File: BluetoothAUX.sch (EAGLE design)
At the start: 17 parts, among them IC2 TPA6132A2, X1 STEREOJACK, X2 MINI-USB-SCHIELD-32005-201

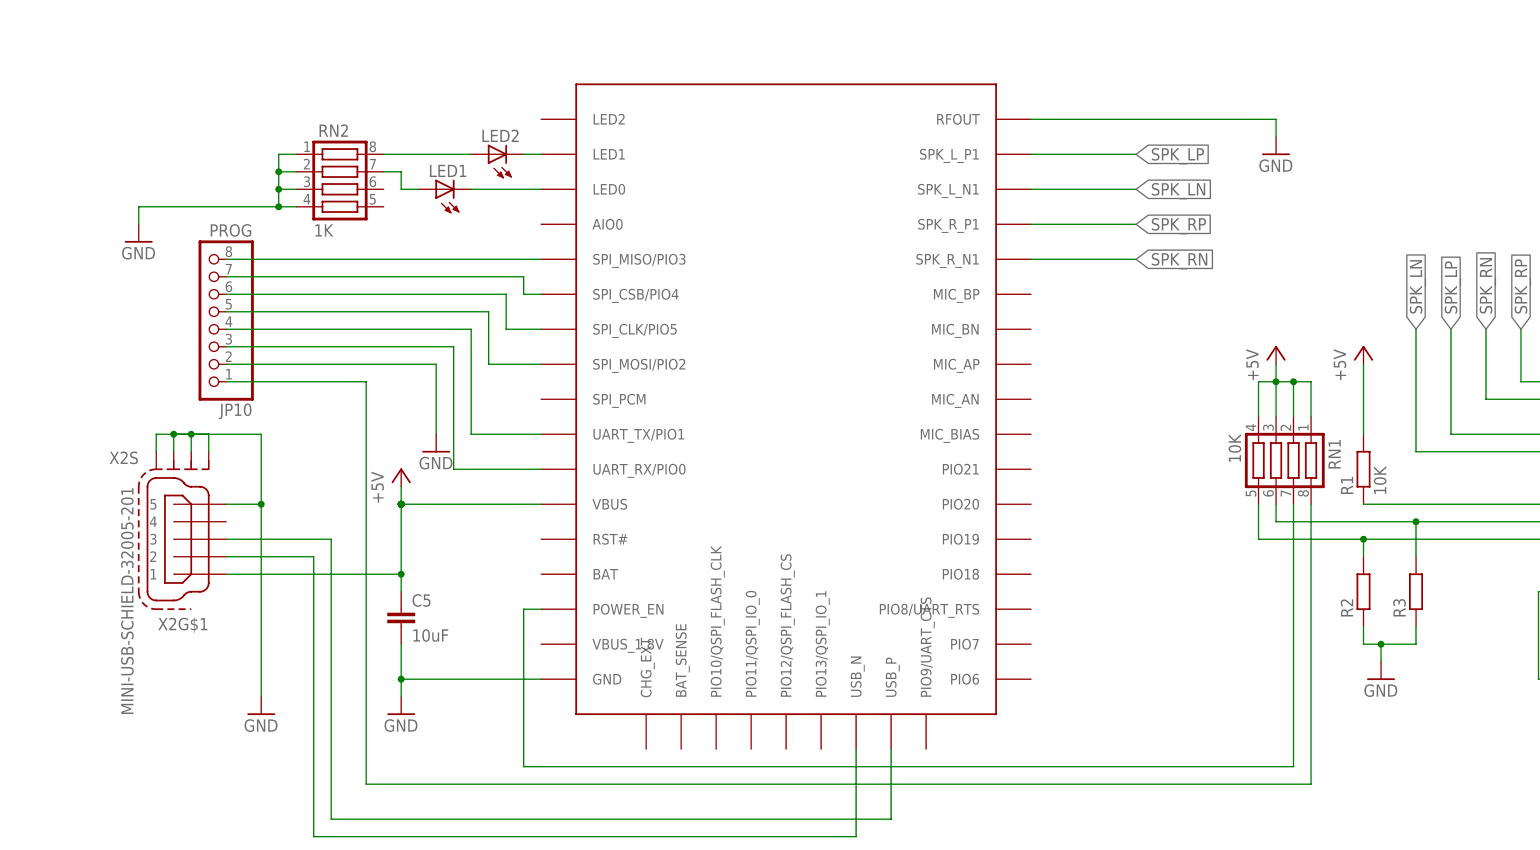
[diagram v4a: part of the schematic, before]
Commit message: Proper RN symbols
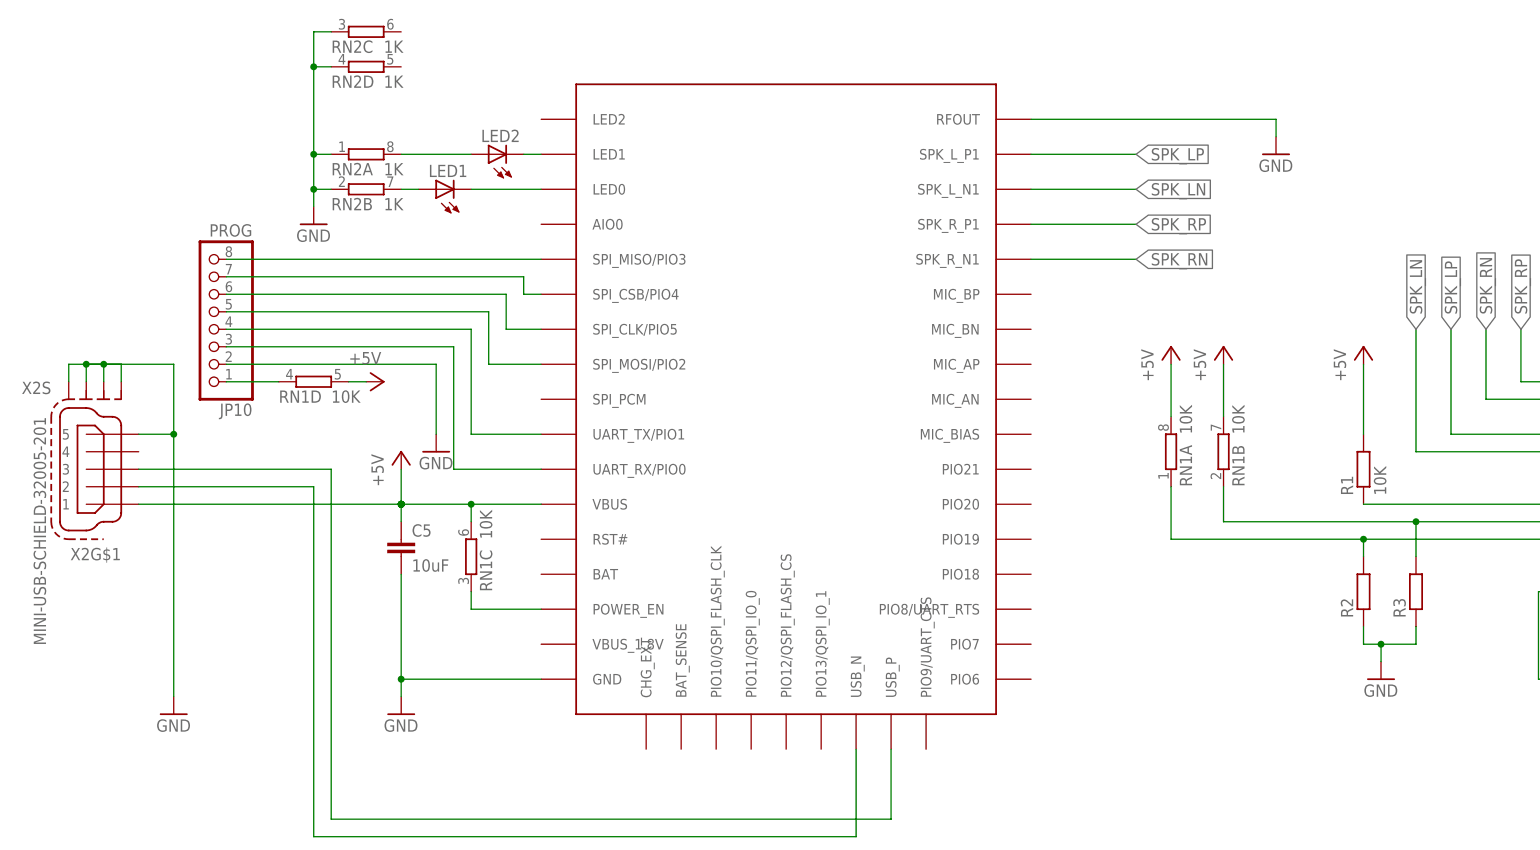
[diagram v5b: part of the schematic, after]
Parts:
- RN1, RN2: device resistor-net:CTS742C083 -> resistor-dil:4R-N0603-ARC
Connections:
- net +5V: now also RN1A.2, RN1B.2, RN1C.2, RN1D.2; no longer RN1.1, RN1.2, RN1.3, RN1.4
- net COM: now also RN1D.1; no longer RN1.8
- net GND: now also RN2A.1, RN2B.1, RN2C.1, RN2D.1; no longer RN2.1, RN2.2, RN2.3, RN2.4
- net LED1-: now also RN2B.2; no longer RN2.7
- net LED2-: now also RN2A.2; no longer RN2.8
- net N$13: now also RN1C.1; no longer RN1.7
- net N$31: now also RN1B.1; no longer RN1.6
- net N$32: now also RN1A.1; no longer RN1.5
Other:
- moved on the sheet: C5, X2G$1, X2S

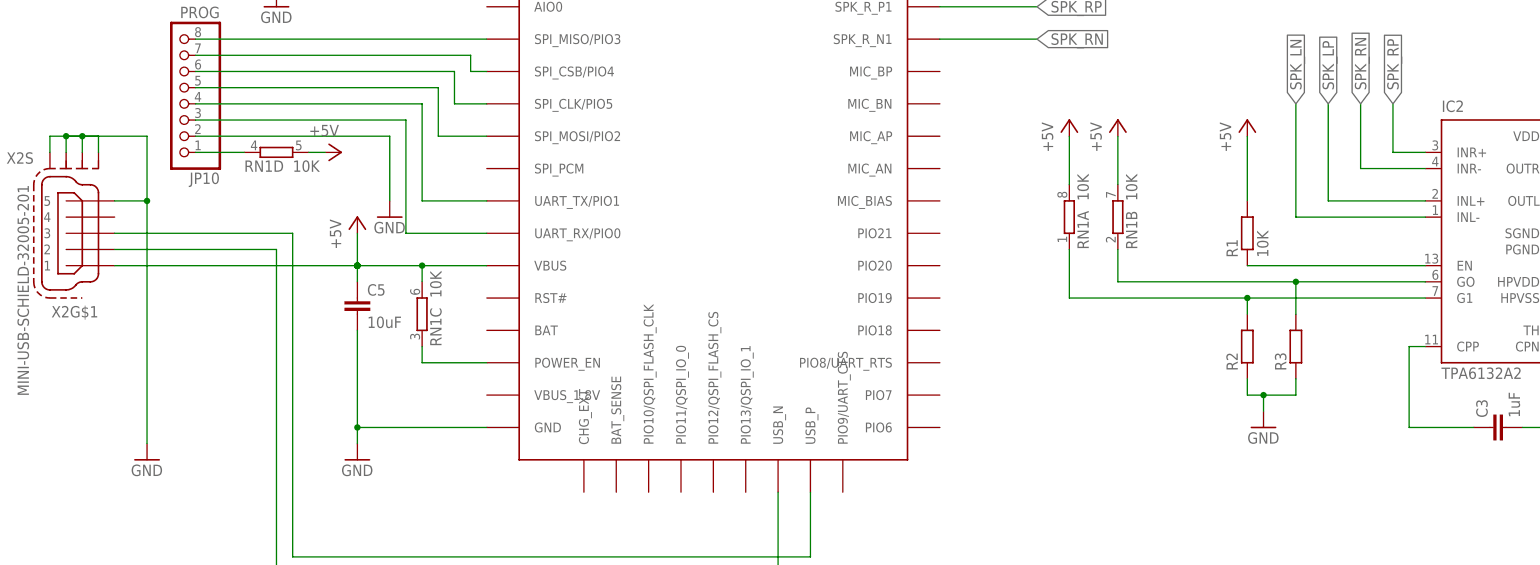
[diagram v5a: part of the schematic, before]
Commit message: Remove unused COM pin
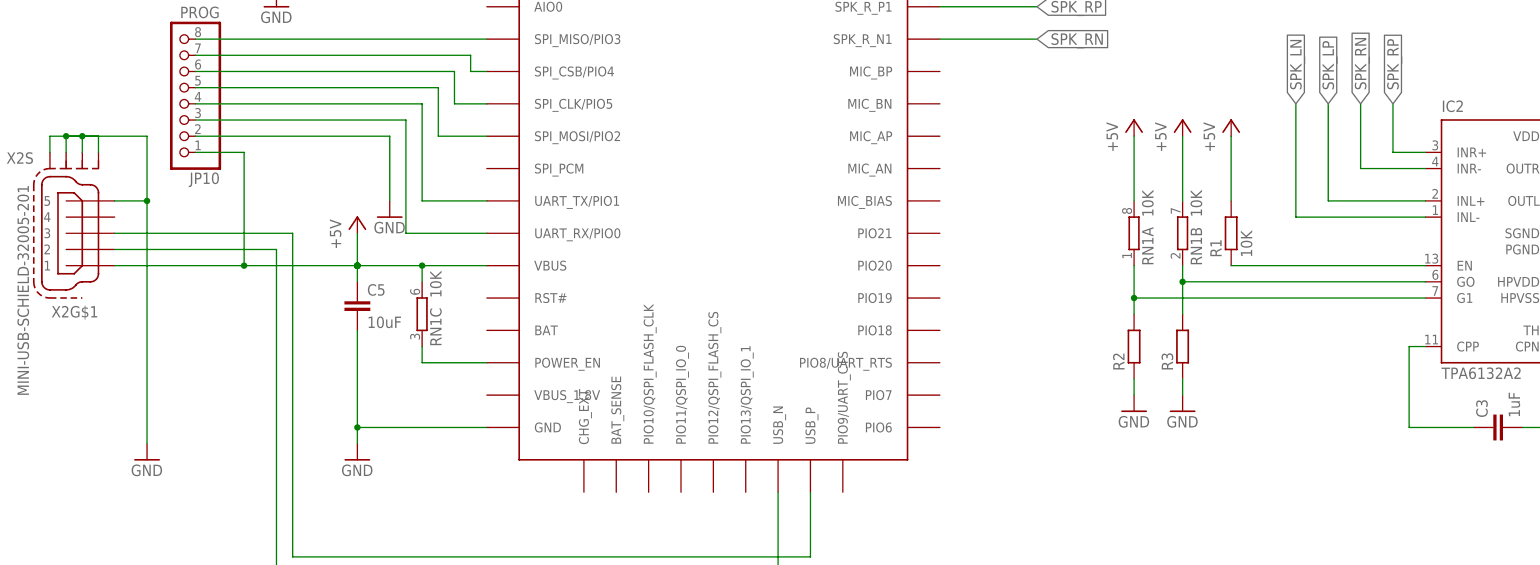
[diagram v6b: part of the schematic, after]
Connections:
- removed net COM: JP10.1, RN1D.1
- net +5V: now also JP10.1; no longer RN1D.2
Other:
- moved on the sheet: R1, R2, R3, RN1A, RN1B
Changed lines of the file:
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@@
 <part name="RN2" library="resistor-dil" library_urn="urn:adsk.eagle:library:342" deviceset="4R-N" device="0603-ARC" package3d_urn="urn:adsk.eagle:package:24926/1" value="1K"/>
 <part name="P+2" library="supply1" deviceset="+5V" device=""/>
-<part name="P+7" library="supply1" deviceset="+5V" device=""/>
+<part name="GND4" library="supply1" deviceset="GND" device=""/>
 </parts>
 <sheets>
@@
 <instance part="GND11" gate="1" x="58.42" y="-33.02"/>
 <instance part="GND12" gate="1" x="68.58" y="-33.02"/>
-<instance part="P+5" gate="1" x="-12.7" y="12.7"/>
-<instance part="P+6" gate="1" x="-33.02" y="12.7"/>
-<instance part="GND14" gate="1" x="-10.16" y="-35.56"/>
-<instance part="R2" gate="G$1" x="-12.7" y="-22.86" rot="R90"/>
-<instance part="R3" gate="G$1" x="-5.08" y="-22.86" rot="R90"/>
+<instance part="P+5" gate="1" x="-15.24" y="12.7"/>
+<instance part="P+6" gate="1" x="-22.86" y="12.7"/>
+<instance part="GND14" gate="1" x="-30.48" y="-33.02"/>
+<instance part="R2" gate="G$1" x="-30.48" y="-22.86" rot="R90"/>
+<instance part="R3" gate="G$1" x="-22.86" y="-22.86" rot="R90"/>
 <instance part="C1" gate="G$1" x="48.26" y="-20.32"/>
 <instance part="C2" gate="G$1" x="58.42" y="-20.32"/>
 <instance part="C3" gate="G$1" x="25.4" y="-35.56" rot="R90"/>
-<instance part="R1" gate="G$1" x="-12.7" y="-5.08" rot="R90"/>
+<instance part="R1" gate="G$1" x="-15.24" y="-5.08" rot="R90"/>
 <instance part="C4" gate="G$1" x="48.26" y="17.78"/>
 <instance part="GND1" gate="1" x="48.26" y="7.62"/>
@@
 <instance part="LED1" gate="G$1" x="-147.32" y="35.56" rot="R90"/>
 <instance part="GND2" gate="1" x="-165.1" y="30.48"/>
-<instance part="RN1" gate="A" x="-40.64" y="-2.54" rot="R90"/>
-<instance part="RN1" gate="B" x="-33.02" y="-2.54" rot="R90"/>
+<instance part="RN1" gate="A" x="-30.48" y="-5.08" rot="R90"/>
+<instance part="RN1" gate="B" x="-22.86" y="-5.08" rot="R90"/>
 <instance part="RN1" gate="C" x="-142.24" y="-17.78" rot="R90"/>
-<instance part="RN1" gate="D" x="-165.1" y="7.62"/>
 <instance part="RN2" gate="A" x="-157.48" y="40.64"/>
 <instance part="RN2" gate="B" x="-157.48" y="35.56"/>
 <instance part="RN2" gate="C" x="-157.48" y="58.42"/>
 <instance part="RN2" gate="D" x="-157.48" y="53.34"/>
-<instance part="P+2" gate="1" x="-40.64" y="12.7"/>
-<instance part="P+7" gate="1" x="-154.94" y="7.62" rot="R270"/>
+<instance part="P+2" gate="1" x="-30.48" y="12.7"/>
+<instance part="GND4" gate="1" x="-22.86" y="-33.02"/>
 </instances>
 <busses>
@@
 <segment>
 <pinref part="GND14" gate="1" pin="GND"/>
-<pinref part="R3" gate="G$1" pin="1"/>
-<wire x1="-10.16" y1="-30.48" x2="-10.16" y2="-33.02" width="0.1524" layer="91"/>
 <pinref part="R2" gate="G$1" pin="1"/>
-<wire x1="-12.7" y1="-27.94" x2="-12.7" y2="-30.48" width="0.1524" layer="91"/>
-<wire x1="-10.16" y1="-30.48" x2="-12.7" y2="-30.48" width="0.1524" layer="91"/>
-<junction x="-10.16" y="-30.48"/>
-<wire x1="-10.16" y1="-30.48" x2="-5.08" y2="-30.48" width="0.1524" layer="91"/>
-<wire x1="-5.08" y1="-30.48" x2="-5.08" y2="-27.94" width="0.1524" layer="91"/>
+<wire x1="-30.48" y1="-27.94" x2="-30.48" y2="-30.48" width="0.1524" layer="91"/>
 </segment>
 <segment>
@@
 <junction x="-165.1" y="53.34"/>
 </segment>
+<segment>
+<pinref part="R3" gate="G$1" pin="1"/>
+<pinref part="GND4" gate="1" pin="GND"/>
+<wire x1="-22.86" y1="-30.48" x2="-22.86" y2="-27.94" width="0.1524" layer="91"/>
+</segment>
 </net>
 <net name="+5V" class="1">
@@
 <segment>
 <pinref part="P+5" gate="1" pin="+5V"/>
-<wire x1="-12.7" y1="10.16" x2="-12.7" y2="0" width="0.1524" layer="91"/>
+<wire x1="-15.24" y1="10.16" x2="-15.24" y2="0" width="0.1524" layer="91"/>
 <pinref part="R1" gate="G$1" pin="2"/>
 </segment>
@@
 <wire x1="-132.08" y1="-10.16" x2="-142.24" y2="-10.16" width="0.1524" layer="91"/>
 <wire x1="-142.24" y1="-10.16" x2="-152.4" y2="-10.16" width="0.1524" layer="91"/>
-<wire x1="-190.5" y1="-10.16" x2="-152.4" y2="-10.16" width="0.1524" layer="91"/>
+<wire x1="-190.5" y1="-10.16" x2="-170.18" y2="-10.16" width="0.1524" layer="91"/>
 <junction x="-152.4" y="-10.16"/>
 <pinref part="P+3" gate="1" pin="+5V"/>
+<wire x1="-170.18" y1="-10.16" x2="-152.4" y2="-10.16" width="0.1524" layer="91"/>
 <wire x1="-152.4" y1="-10.16" x2="-152.4" y2="-5.08" width="0.1524" layer="91"/>
 <wire x1="-142.24" y1="-12.7" x2="-142.24" y2="-10.16" width="0.1524" layer="91"/>
 <junction x="-142.24" y="-10.16"/>
+<pinref part="JP10" gate="A" pin="1"/>
+<wire x1="-177.8" y1="7.62" x2="-170.18" y2="7.62" width="0.1524" layer="91"/>
+<wire x1="-170.18" y1="7.62" x2="-170.18" y2="-10.16" width="0.1524" layer="91"/>
+<junction x="-170.18" y="-10.16"/>
 </segment>
 <segment>
 <pinref part="RN1" gate="A" pin="2"/>
-<wire x1="-40.64" y1="10.16" x2="-40.64" y2="2.54" width="0.1524" layer="91"/>
+<wire x1="-30.48" y1="10.16" x2="-30.48" y2="0" width="0.1524" layer="91"/>
 <pinref part="P+2" gate="1" pin="+5V"/>
-</segment>
-<segment>
-<pinref part="RN1" gate="D" pin="2"/>
-<pinref part="P+7" gate="1" pin="+5V"/>
-<wire x1="-157.48" y1="7.62" x2="-160.02" y2="7.62" width="0.1524" layer="91"/>
 </segment>
 <segment>
 <pinref part="P+6" gate="1" pin="+5V"/>
 <pinref part="RN1" gate="B" pin="2"/>
-<wire x1="-33.02" y1="2.54" x2="-33.02" y2="10.16" width="0.1524" layer="91"/>
+<wire x1="-22.86" y1="0" x2="-22.86" y2="10.16" width="0.1524" layer="91"/>
 </segment>
 </net>
@@
 <wire x1="-142.24" y1="-25.4" x2="-142.24" y2="-22.86" width="0.1524" layer="91"/>
 <pinref part="RN1" gate="C" pin="1"/>
-</segment>
-</net>
-<net name="COM" class="0">
-<segment>
-<pinref part="JP10" gate="A" pin="1"/>
-<wire x1="-177.8" y1="7.62" x2="-170.18" y2="7.62" width="0.1524" layer="91"/>
-<pinref part="RN1" gate="D" pin="1"/>
 </segment>
 </net>
@@
 <segment>
 <pinref part="IC2" gate="G$1" pin="EN"/>
-<wire x1="-12.7" y1="-10.16" x2="15.24" y2="-10.16" width="0.1524" layer="91"/>
+<wire x1="-15.24" y1="-10.16" x2="15.24" y2="-10.16" width="0.1524" layer="91"/>
 <pinref part="R1" gate="G$1" pin="1"/>
 </segment>
@@
 <pinref part="IC2" gate="G$1" pin="GO"/>
 <pinref part="R3" gate="G$1" pin="2"/>
-<wire x1="-5.08" y1="-12.7" x2="15.24" y2="-12.7" width="0.1524" layer="91"/>
-<wire x1="-5.08" y1="-17.78" x2="-5.08" y2="-12.7" width="0.1524" layer="91"/>
-<junction x="-5.08" y="-12.7"/>
-<wire x1="-5.08" y1="-12.7" x2="-33.02" y2="-12.7" width="0.1524" layer="91"/>
+<wire x1="-22.86" y1="-12.7" x2="15.24" y2="-12.7" width="0.1524" layer="91"/>
+<wire x1="-22.86" y1="-17.78" x2="-22.86" y2="-12.7" width="0.1524" layer="91"/>
+<junction x="-22.86" y="-12.7"/>
 <pinref part="RN1" gate="B" pin="1"/>
-<wire x1="-33.02" y1="-12.7" x2="-33.02" y2="-7.62" width="0.1524" layer="91"/>
+<wire x1="-22.86" y1="-12.7" x2="-22.86" y2="-10.16" width="0.1524" layer="91"/>
 </segment>
 </net>
@@
 <segment>
 <pinref part="IC2" gate="G$1" pin="G1"/>
-<wire x1="-12.7" y1="-15.24" x2="-12.7" y2="-17.78" width="0.1524" layer="91"/>
-<wire x1="-12.7" y1="-15.24" x2="15.24" y2="-15.24" width="0.1524" layer="91"/>
+<wire x1="-30.48" y1="-15.24" x2="-30.48" y2="-17.78" width="0.1524" layer="91"/>
+<wire x1="-30.48" y1="-15.24" x2="15.24" y2="-15.24" width="0.1524" layer="91"/>
 <pinref part="R2" gate="G$1" pin="2"/>
-<wire x1="-12.7" y1="-15.24" x2="-40.64" y2="-15.24" width="0.1524" layer="91"/>
-<junction x="-12.7" y="-15.24"/>
+<junction x="-30.48" y="-15.24"/>
 <pinref part="RN1" gate="A" pin="1"/>
-<wire x1="-40.64" y1="-15.24" x2="-40.64" y2="-7.62" width="0.1524" layer="91"/>
-</segment>
-</net>
+<wire x1="-30.48" y1="-15.24" x2="-30.48" y2="-10.16" width="0.1524" layer="91"/>
+</segment>
+</net>

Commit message: Make smaller
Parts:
- removed LED2: (no value), led:LED3MM
- removed R1: 10K, resistor:R-EU_R0603
- removed X1: STEREOJACK, adafruit:STEREOJACK
- removed X2: MINI-USB-SCHIELD-32005-201, con-cypressindustries:MINI-USB-SCHIELD-32005-201
- added J3: AUDIO_JACK_TRRSSMD_RA, SparkFun-Connectors:AUDIO_JACK_TRRSSMD_RA
- added J4: USB, SparkFun-Connectors:USB_MICRO-B_SMT
- LED1: value (none) -> RGBLED5050; device led:LED3MM -> adafruit:RGBLED5050
- R2, R3: value (none) -> 0
- RN2: value 1K -> 220
- U$1: device BT:F3188 -> BluetoothAUX:F3188
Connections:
- net N$26 renamed CPP
- net N$27 renamed CPN
- net N$28 renamed HPVSS
- net N$29 renamed HVPDD
- net N$31 renamed G0
- net N$32 renamed G1
- removed net LED1+: LED1.C, U$1.LED0
- removed net LED1-: LED1.A, RN2B.2
- removed net LED2+: LED2.C, U$1.LED1
- removed net LED2-: LED2.A, RN2A.2
- removed net N$13: RN1C.1, U$1.POWER_EN
- removed net N$14: IC2.OUTR, X1.2
- removed net N$18: U$1.USB_N, X2G$1.2
- removed net N$19: U$1.USB_P, X2G$1.3
- removed net N$20: IC2.OUTL, X1.5
- removed net N$30: IC2.EN, R1.1
- new net LED0: LED1.BLUE_C, U$1.LED0
- new net LED1: LED1.RED_C, U$1.LED1
- new net LED2: LED1.GREEN_C, U$1.LED2
- new net LED_B: LED1.BLUE_A, RN2D.2
- new net LED_G: LED1.GREEN_A, RN2A.2
- new net LED_R: LED1.RED_A, RN2B.2
- new net OUTL: IC2.OUTL, J3.TIP
- new net OUTR: IC2.OUTR, J3.RING1
- new net POWER_EN: RN1D.1, U$1.POWER_EN
- new net TPA_EN: IC2.EN, RN1C.1
- new net USB_N: J4.D-, U$1.USB_N
- new net USB_P: J4.D+, U$1.USB_P
- net +5V: now also J4.VBUS, RN1D.2; no longer R1.2, X2G$1.1
- net GND: now also J4.GND, J4.SHIELD; no longer X2G$1.5, X2S.S1, X2S.S2, X2S.S3, X2S.S4
- net SGND: now also J3.EARTH; no longer X1.1
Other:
- moved on the sheet: RN1A, RN1B, RN1C, RN2A, RN2B, RN2C, RN2D

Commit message: Make smaller
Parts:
- removed JP10: PROG, pinhead:PINHD-1X8
- added JP1: PROG, pinhead:PINHD-1X7
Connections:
- net USB_N renamed USBN
- net USB_P renamed USBP
- net +5V: no longer JP10.1
- net CLK: now also JP1.5; no longer JP10.6
- net CS: now also JP1.6; no longer JP10.7
- net G0: now also RN1C.1; no longer RN1B.1
- net G1: now also RN1B.1; no longer RN1A.1
- net GND: now also IC2.TH, JP1.1; no longer JP10.2
- net MISO: now also JP1.7; no longer JP10.8
- net MOSI: now also JP1.4; no longer JP10.5
- net RX: now also JP1.2; no longer JP10.3
- net TPA_EN: now also RN1A.1; no longer RN1C.1
- net TX: now also JP1.3; no longer JP10.4
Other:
- moved on the sheet: C1, C2, RN1A, RN1B, RN1C
